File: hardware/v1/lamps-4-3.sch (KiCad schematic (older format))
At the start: 10 parts, among them P1 CONN_01X04, P2 CONN_01X04, P3 CONN_02X05

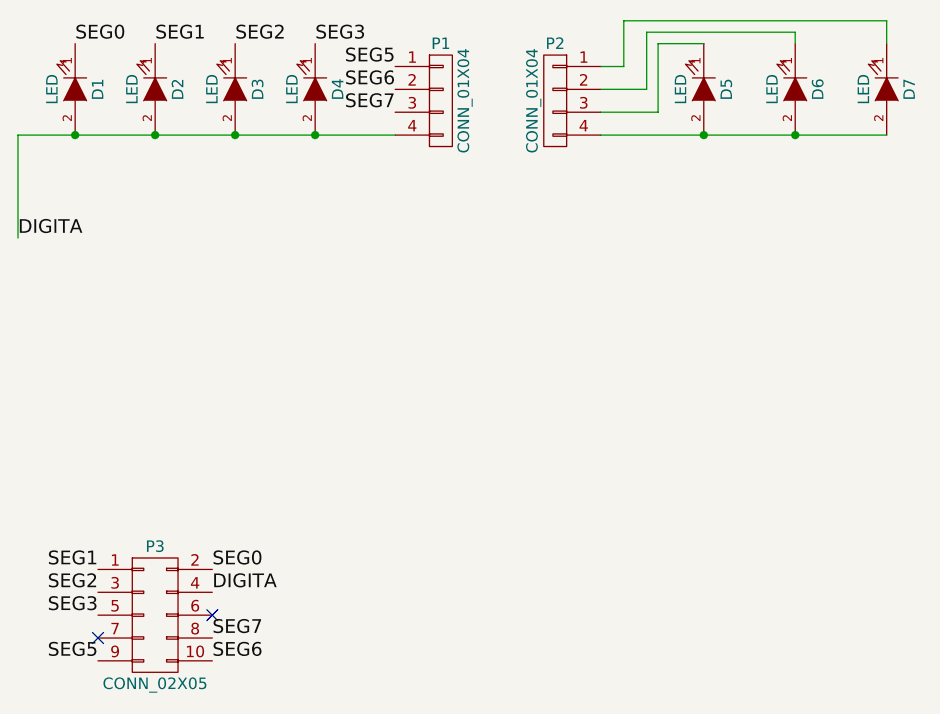
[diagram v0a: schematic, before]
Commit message: Add pcbs and cutouts for magnetic drum store status lamps (not labelled).
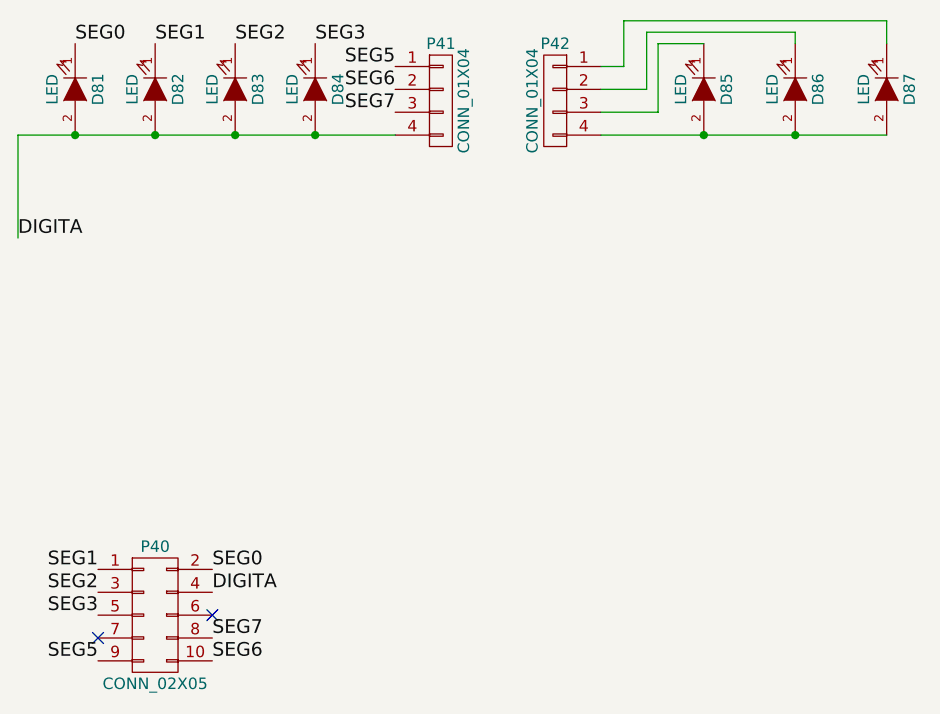
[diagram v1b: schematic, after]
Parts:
- renumbered D1 to D81, D2 to D82, D3 to D83, D4 to D84, D5 to D85, D6 to D86, D7 to D87, P3 to P40, P1 to P41, P2 to P42
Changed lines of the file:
@@
 LIBS:contrib
 LIBS:valves
-LIBS:lamps-4-3-cache
+LIBS:MAX7221
+LIBS:MCP23S17
+LIBS:MCP23017
+LIBS:Pi2_Connector
+LIBS:v1-cache
 EELAYER 25 0
 EELAYER END
 $Descr A4 11693 8268
 encoding utf-8
-Sheet 1 1
+Sheet 1 36
 Title ""
 Date ""
@@
 $EndDescr
 $Comp
-L LED D1
+L LED D81
 U 1 1 57AB5D5D
 P 2200 1800
-F 0 "D1" H 2200 1900 50  0000 C CNN
+F 0 "D81" H 2200 1900 50  0000 C CNN
 F 1 "LED" H 2200 1700 50  0000 C CNN
 F 2 "myparts:LED-5MM-custom" H 2200 1800 50  0001 C CNN
@@
 $EndComp
 $Comp
-L LED D2
+L LED D82
 U 1 1 57AB5DB1
 P 2550 1800
-F 0 "D2" H 2550 1900 50  0000 C CNN
+F 0 "D82" H 2550 1900 50  0000 C CNN
 F 1 "LED" H 2550 1700 50  0000 C CNN
 F 2 "myparts:LED-5MM-custom" H 2550 1800 50  0001 C CNN
@@
 $EndComp
 $Comp
-L LED D3
+L LED D83
 U 1 1 57AB5DCA
 P 2900 1800
-F 0 "D3" H 2900 1900 50  0000 C CNN
+F 0 "D83" H 2900 1900 50  0000 C CNN
 F 1 "LED" H 2900 1700 50  0000 C CNN
 F 2 "myparts:LED-5MM-custom" H 2900 1800 50  0001 C CNN
@@
 $EndComp
 $Comp
-L LED D4
+L LED D84
 U 1 1 57AB5DE8
 P 3250 1800
-F 0 "D4" H 3250 1900 50  0000 C CNN
+F 0 "D84" H 3250 1900 50  0000 C CNN
 F 1 "LED" H 3250 1700 50  0000 C CNN
 F 2 "myparts:LED-5MM-custom" H 3250 1800 50  0001 C CNN
@@
 $EndComp
 $Comp
-L LED D5
+L LED D85
 U 1 1 57AB5E41
 P 4950 1800
-F 0 "D5" H 4950 1900 50  0000 C CNN
+F 0 "D85" H 4950 1900 50  0000 C CNN
 F 1 "LED" H 4950 1700 50  0000 C CNN
 F 2 "myparts:LED-5MM-custom" H 4950 1800 50  0001 C CNN
@@
 $EndComp
 $Comp
-L LED D6
+L LED D86
 U 1 1 57AB5E6E
 P 5350 1800
-F 0 "D6" H 5350 1900 50  0000 C CNN
+F 0 "D86" H 5350 1900 50  0000 C CNN
 F 1 "LED" H 5350 1700 50  0000 C CNN
 F 2 "myparts:LED-5MM-custom" H 5350 1800 50  0001 C CNN
@@
 $EndComp
 $Comp
-L LED D7
+L LED D87
 U 1 1 57AB5E94
 P 5750 1800
-F 0 "D7" H 5750 1900 50  0000 C CNN
+F 0 "D87" H 5750 1900 50  0000 C CNN
 F 1 "LED" H 5750 1700 50  0000 C CNN
 F 2 "myparts:LED-5MM-custom" H 5750 1800 50  0001 C CNN
@@
 Connection ~ 3250 2000
 $Comp
-L CONN_01X04 P1
+L CONN_01X04 P41
 U 1 1 57AB6038
 P 3800 1850
-F 0 "P1" H 3800 2100 50  0000 C CNN
+F 0 "P41" H 3800 2100 50  0000 C CNN
 F 1 "CONN_01X04" V 3900 1850 50  0000 C CNN
 F 2 "Pin_Headers:Pin_Header_Angled_1x04" H 3800 1850 50  0001 C CNN
@@
 $EndComp
 $Comp
-L CONN_01X04 P2
+L CONN_01X04 P42
 U 1 1 57AB6070
 P 4300 1850
-F 0 "P2" H 4300 2100 50  0000 C CNN
+F 0 "P42" H 4300 2100 50  0000 C CNN
 F 1 "CONN_01X04" V 4400 1850 50  0000 C CNN
 F 2 "Pin_Headers:Pin_Header_Angled_1x04" H 4300 1850 50  0001 C CNN
@@
 SEG3
 $Comp
-L CONN_02X05 P3
+L CONN_02X05 P40
 U 1 1 57AB7B49
 P 2550 4100
-F 0 "P3" H 2550 4400 50  0000 C CNN
+F 0 "P40" H 2550 4400 50  0000 C CNN
 F 1 "CONN_02X05" H 2550 3800 50  0000 C CNN
 F 2 "Pin_Headers:Pin_Header_Straight_2x05" H 2550 2900 50  0001 C CNN
